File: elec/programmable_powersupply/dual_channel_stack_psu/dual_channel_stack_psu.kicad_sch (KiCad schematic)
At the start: 40 parts, among them J1 Conn_01x03_Pin, J2 Conn_01x05, Q1 Q_NMOS_GDS, Q2 Q_NMOS_GDS

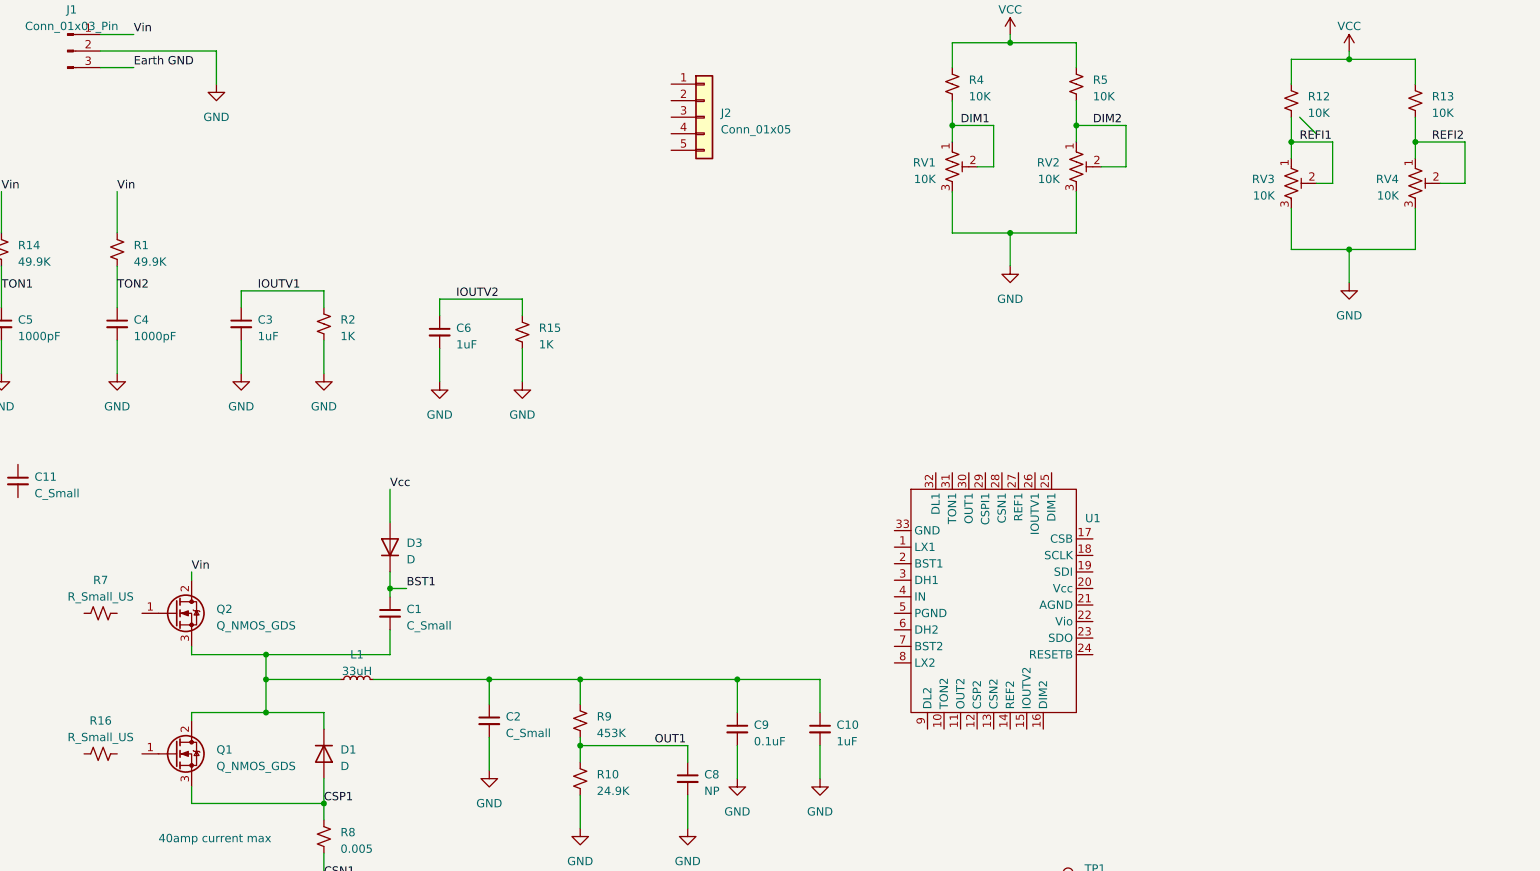
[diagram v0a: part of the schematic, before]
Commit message: added P&ID control diagram and updated dual channel stack psu
Signed-off-by: lokimetasmith <lokimail@gmail.com>
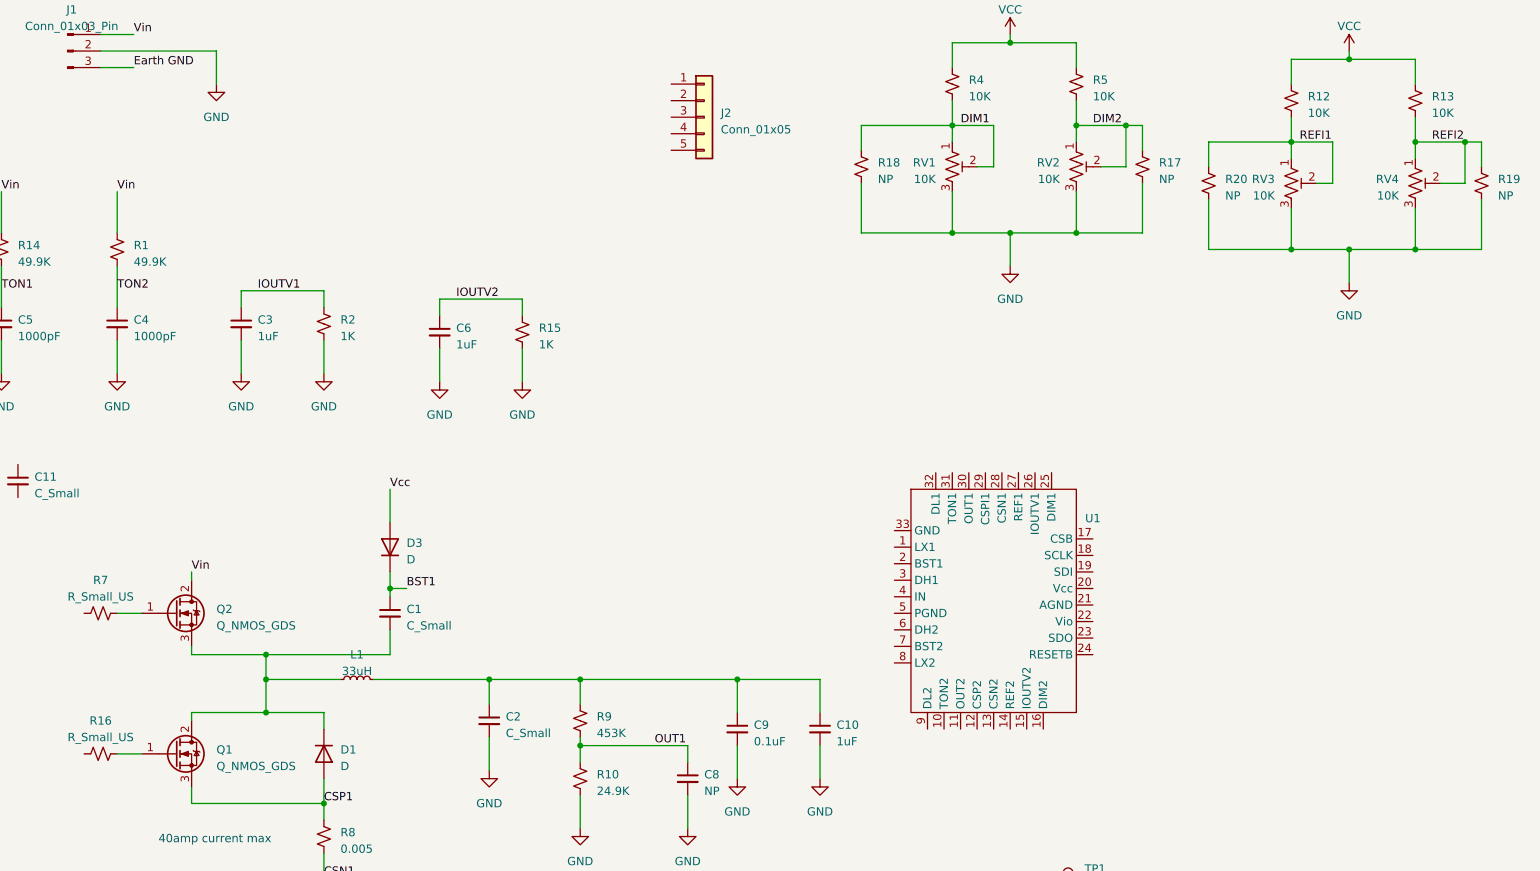
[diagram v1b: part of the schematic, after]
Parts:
- added R17, R18, R19, R20: NP, symbol Device:R_Small_US
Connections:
- net DIM1: now also R18.1
- net DIM2: now also R17.1
- net GND: now also R17.2, R18.2, R19.2, R20.2
- net REFI1: now also R20.1
- net REFI2: now also R19.1
- net at Q2.1 (G): now also R7.2
- net at R16.2: now also Q1.1 (G)
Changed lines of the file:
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@@
   (junction (at 217.17 38.1) (diameter 0) (color 0 0 0 0)
   )
+  (junction (at 191.77 35.56) (diameter 0) (color 0 0 0 0)
+  )
   (junction (at 107.95 130.81) (diameter 0) (color 0 0 0 0)
   )
@@
   (junction (at 59.69 116.84) (diameter 0) (color 0 0 0 0)
   )
+  (junction (at 236.22 54.61) (diameter 0) (color 0 0 0 0)
+  )
   (junction (at 132.08 120.65) (diameter 0) (color 0 0 0 0)
   )
   (junction (at 59.69 120.65) (diameter 0) (color 0 0 0 0)
   )
+  (junction (at 184.15 52.07) (diameter 0) (color 0 0 0 0)
+  )
   (junction (at 173.99 52.07) (diameter 0) (color 0 0 0 0)
   )
+  (junction (at 243.84 38.1) (diameter 0) (color 0 0 0 0)
+  )
   (junction (at 236.22 38.1) (diameter 0) (color 0 0 0 0)
   )
+  (junction (at 217.17 54.61) (diameter 0) (color 0 0 0 0)
+  )
   (junction (at 184.15 35.56) (diameter 0) (color 0 0 0 0)
   )
   (junction (at 173.99 22.86) (diameter 0) (color 0 0 0 0)
   )
+  (junction (at 165.1 52.07) (diameter 0) (color 0 0 0 0)
+  )
   (junction (at 59.69 125.73) (diameter 0) (color 0 0 0 0)
   )
   (junction (at 165.1 35.56) (diameter 0) (color 0 0 0 0)
   )
-  (bus_entry (at 218.44 34.29) (size 2.54 2.54)
-    (stroke (width 0) (type default))
-  )
   (wire (pts (xy 191.77 41.91) (xy 187.96 41.91))
     (stroke (width 0) (type default))
   )
+  (wire (pts (xy 194.31 52.07) (xy 184.15 52.07))
+    (stroke (width 0) (type default))
+  )
   (wire (pts (xy 124.46 133.35) (xy 124.46 130.81))
     (stroke (width 0) (type default))
@@
     (stroke (width 0) (type default))
   )
+  (wire (pts (xy 151.13 44.45) (xy 151.13 52.07))
+    (stroke (width 0) (type default))
+  )
   (wire (pts (xy 107.95 130.81) (xy 107.95 133.35))
     (stroke (width 0) (type default))
@@
     (stroke (width 0) (type default))
   )
+  (wire (pts (xy 204.47 46.99) (xy 204.47 54.61))
+    (stroke (width 0) (type default))
+  )
   (wire (pts (xy 99.06 64.77) (xy 99.06 62.23))
     (stroke (width 0) (type default))
@@
     (stroke (width 0) (type default))
   )
+  (wire (pts (xy 151.13 35.56) (xy 151.13 39.37))
+    (stroke (width 0) (type default))
+  )
   (wire (pts (xy 68.58 147.32) (xy 68.58 152.4))
     (stroke (width 0) (type default))
@@
     (stroke (width 0) (type default))
   )
+  (wire (pts (xy 246.38 38.1) (xy 246.38 41.91))
+    (stroke (width 0) (type default))
+  )
   (wire (pts (xy 226.06 54.61) (xy 226.06 59.69))
     (stroke (width 0) (type default))
@@
     (stroke (width 0) (type default))
   )
+  (wire (pts (xy 194.31 44.45) (xy 194.31 52.07))
+    (stroke (width 0) (type default))
+  )
   (wire (pts (xy 223.52 44.45) (xy 223.52 38.1))
     (stroke (width 0) (type default))
@@
     (stroke (width 0) (type default))
   )
+  (wire (pts (xy 236.22 54.61) (xy 246.38 54.61))
+    (stroke (width 0) (type default))
+  )
+  (wire (pts (xy 204.47 38.1) (xy 204.47 41.91))
+    (stroke (width 0) (type default))
+  )
   (wire (pts (xy 48.26 125.73) (xy 59.69 125.73))
     (stroke (width 0) (type default))
@@
     (stroke (width 0) (type default))
   )
+  (wire (pts (xy 204.47 38.1) (xy 217.17 38.1))
+    (stroke (width 0) (type default))
+  )
   (wire (pts (xy 184.15 52.07) (xy 173.99 52.07))
     (stroke (width 0) (type default))
@@
     (stroke (width 0) (type default))
   )
+  (wire (pts (xy 36.83 110.49) (xy 40.64 110.49))
+    (stroke (width 0) (type default))
+  )
   (wire (pts (xy 78.74 116.84) (xy 78.74 113.03))
     (stroke (width 0) (type default))
@@
     (stroke (width 0) (type default))
   )
+  (wire (pts (xy 243.84 38.1) (xy 246.38 38.1))
+    (stroke (width 0) (type default))
+  )
   (wire (pts (xy 59.69 116.84) (xy 48.26 116.84))
     (stroke (width 0) (type default))
@@
     (stroke (width 0) (type default))
   )
+  (wire (pts (xy 191.77 35.56) (xy 194.31 35.56))
+    (stroke (width 0) (type default))
+  )
+  (wire (pts (xy 246.38 46.99) (xy 246.38 54.61))
+    (stroke (width 0) (type default))
+  )
   (wire (pts (xy 165.1 26.67) (xy 165.1 22.86))
     (stroke (width 0) (type default))
@@
     (stroke (width 0) (type default))
   )
+  (wire (pts (xy 194.31 35.56) (xy 194.31 39.37))
+    (stroke (width 0) (type default))
+  )
   (wire (pts (xy 132.08 130.81) (xy 132.08 135.89))
     (stroke (width 0) (type default))
   )
+  (wire (pts (xy 151.13 52.07) (xy 165.1 52.07))
+    (stroke (width 0) (type default))
+  )
   (wire (pts (xy 184.15 45.72) (xy 184.15 52.07))
     (stroke (width 0) (type default))
@@
     (stroke (width 0) (type default))
   )
+  (wire (pts (xy 151.13 35.56) (xy 165.1 35.56))
+    (stroke (width 0) (type default))
+  )
   (wire (pts (xy 226.06 24.13) (xy 226.06 25.4))
     (stroke (width 0) (type default))
@@
     (stroke (width 0) (type default))
   )
+  (wire (pts (xy 204.47 54.61) (xy 217.17 54.61))
+    (stroke (width 0) (type default))
+  )
   (wire (pts (xy 93.98 129.54) (xy 93.98 134.62))
     (stroke (width 0) (type default))
@@
   )
   (wire (pts (xy 86.36 69.85) (xy 86.36 74.93))
+    (stroke (width 0) (type default))
+  )
+  (wire (pts (xy 36.83 132.08) (xy 40.64 132.08))
     (stroke (width 0) (type default))
   )
@@
     )
   )
+  (symbol (lib_id "Device:R_Small_US") (at 194.31 41.91 0) (unit 1)
+    (in_bom yes) (on_board yes) (dnp no) (fields_autoplaced)
+    (property "Reference" "R17" (at 196.85 41.275 0)
+      (effects (font (size 1.27 1.27)) (justify left))
+    )
+    (property "Value" "NP" (at 196.85 43.815 0)
+      (effects (font (size 1.27 1.27)) (justify left))
+    )
+    (property "Footprint" "" (at 194.31 41.91 0)
+      (effects (font (size 1.27 1.27)) hide)
+    )
+    (property "Datasheet" "~" (at 194.31 41.91 0)
+      (effects (font (size 1.27 1.27)) hide)
+    )
+    (pin "1")
+    (pin "2")
+    (instances
+      (project "dual_channel_stack_psu"
+        (path "/8f6d02f7-7b5e-4155-bbdb-2d46789ca027"
+          (reference "R17") (unit 1)
+        )
+      )
+    )
+  )
   (symbol (lib_id "Device:R_Small_US") (at 36.83 54.61 0) (unit 1)
     (in_bom yes) (on_board yes) (dnp no) (fields_autoplaced)
@@
     )
   )
+  (symbol (lib_id "Device:R_Small_US") (at 151.13 41.91 0) (unit 1)
+    (in_bom yes) (on_board yes) (dnp no) (fields_autoplaced)
+    (property "Reference" "R18" (at 153.67 41.275 0)
+      (effects (font (size 1.27 1.27)) (justify left))
+    )
+    (property "Value" "NP" (at 153.67 43.815 0)
+      (effects (font (size 1.27 1.27)) (justify left))
+    )
+    (property "Footprint" "" (at 151.13 41.91 0)
+      (effects (font (size 1.27 1.27)) hide)
+    )
+    (property "Datasheet" "~" (at 151.13 41.91 0)
+      (effects (font (size 1.27 1.27)) hide)
+    )
+    (pin "1")
+    (pin "2")
+    (instances
+      (project "dual_channel_stack_psu"
+        (path "/8f6d02f7-7b5e-4155-bbdb-2d46789ca027"
+          (reference "R18") (unit 1)
+        )
+      )
+    )
+  )
   (symbol (lib_id "Device:C_Small") (at 55.88 66.04 0) (unit 1)
     (in_bom yes) (on_board yes) (dnp no) (fields_autoplaced)
@@
         (path "/8f6d02f7-7b5e-4155-bbdb-2d46789ca027"
           (reference "#PWR015") (unit 1)
+        )
+      )
+    )
+  )
+  (symbol (lib_id "Device:R_Small_US") (at 246.38 44.45 0) (unit 1)
+    (in_bom yes) (on_board yes) (dnp no) (fields_autoplaced)
+    (property "Reference" "R19" (at 248.92 43.815 0)
+      (effects (font (size 1.27 1.27)) (justify left))
+    )
+    (property "Value" "NP" (at 248.92 46.355 0)
+      (effects (font (size 1.27 1.27)) (justify left))
+    )
+    (property "Footprint" "" (at 246.38 44.45 0)
+      (effects (font (size 1.27 1.27)) hide)
+    )
+    (property "Datasheet" "~" (at 246.38 44.45 0)
+      (effects (font (size 1.27 1.27)) hide)
+    )
+    (pin "1")
+    (pin "2")
+    (instances
+      (project "dual_channel_stack_psu"
+        (path "/8f6d02f7-7b5e-4155-bbdb-2d46789ca027"
+          (reference "R19") (unit 1)
         )
       )
@@
         )
       )
+    )
+  )
+  (symbol (lib_id "Device:R_Small_US") (at 204.47 44.45 0) (unit 1)
+    (in_bom yes) (on_board yes) (dnp no) (fields_autoplaced)
+    (property "Reference" "R20" (at 207.01 43.815 0)
+      (effects (font (size 1.27 1.27)) (justify left))
+    )
+    (property "Value" "NP" (at 207.01 46.355 0)
+      (effects (font (size 1.27 1.27)) (justify left))
+    )
+    (property "Footprint" "" (at 204.47 44.45 0)
+      (effects (font (size 1.27 1.27)) hide)
+    )
+    (property "Datasheet" "~" (at 204.47 44.45 0)
+      (effects (font (size 1.27 1.27)) hide)
+    )
+    (pin "1")
+    (pin "2")
+    (instances
+      (project "dual_channel_stack_psu"
+        (path "/8f6d02f7-7b5e-4155-bbdb-2d46789ca027"
+          (reference "R20") (unit 1)
+        )
+      )

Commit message: updated SBC setup instructions
Signed-off-by: lokimetasmith <lokimail@gmail.com>
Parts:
- added J10, J3, J6, J7: Conn_01x10, Connector_PinSocket_2.54mm:PinSocket_1x10_P2.54mm_Vertical, symbol Connector_Generic:Conn_01x10
- added J4, J8: Conn_02x12_Odd_Even, PubInv_KiCad_PCB.pretty:PinHeader_2x12_P2.00mm_Vertical_JST, symbol Connector_Generic:Conn_02x12_Odd_Even
- added J5, J9: Screw_Terminal_01x02, TerminalBlock_TE-Connectivity:TerminalBlock_TE_282834-2_1x02_P2.54mm_Horizontal, symbol Connector:Screw_Terminal_01x02
- added JP1, JP2: SolderJumper_2_Open, symbol Jumper:SolderJumper_2_Open
- added Q601 (x2): BSS138, Package_TO_SOT_SMD:SOT-23, symbol Transistor_FET:BSS138
- added R101 (x12): 1R0, Resistor_SMD:R_0603_1608Metric_Pad0.98x0.95mm_HandSolder, symbol Device:R
- added R102 (x2): 10K, Resistor_SMD:R_0603_1608Metric_Pad0.98x0.95mm_HandSolder, symbol Device:R
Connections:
- net GND: now also J3.2 (Pin_2), J3.3 (Pin_3), J3.5 (Pin_5), J3.7 (Pin_7), J3.8 (Pin_8), J3.9 (Pin_9), J4.10 (Pin_10), J4.14 (Pin_14), J4.16 (Pin_16), J4.18 (Pin_18), J4.22 (Pin_22), J4.4 (Pin_4), J4.6 (Pin_6), J7.3 (Pin_3), J7.5 (Pin_5), J7.7 (Pin_7), J7.8 (Pin_8), J7.9 (Pin_9), J8.10 (Pin_10), J8.14 (Pin_14), J8.16 (Pin_16), J8.18 (Pin_18), J8.22 (Pin_22), J8.6 (Pin_6), Q601.2 (S), Q601.2 (S), R102.2, R102.2
- net VO+: now reaches C10.1, C2.1, C9.1, L1.2
- net VO+: now also J3.1 (Pin_1), J4.2 (Pin_2), JP1.2 (B); no longer R9.1
- new net: Q601.1 (G), R102.1
- new net ACI: J4.13 (Pin_13), J6.7 (Pin_7)
- new net ACI2: J10.7 (Pin_7), J8.13 (Pin_13)
- new net AUX: J3.6 (Pin_6), J4.12 (Pin_12), J4.17 (Pin_17), J4.21 (Pin_21), J6.10 (Pin_10), J6.9 (Pin_9), R101.1
- new net AUX2: J10.10 (Pin_10), J10.9 (Pin_9), J7.6 (Pin_6), J8.12 (Pin_12), J8.17 (Pin_17), J8.21 (Pin_21), R101.1
- new net D_PSU_RX: R101.2
- new net D_PSU_RX2: R101.2
- new net D_PSU_TX: R101.1
- new net D_PSU_TX2: R101.1
- new net EN+: J4.11 (Pin_11), J6.6 (Pin_6), R101.2
- new net EN-: J4.9 (Pin_9), J6.5 (Pin_5), Q601.3 (D)
- new net EN2+: J10.6 (Pin_6), J8.11 (Pin_11), R101.2
- new net EN2-: J10.5 (Pin_5), J8.9 (Pin_9), Q601.3 (D)
- new net PAR: J4.7 (Pin_7), J6.4 (Pin_4)
- new net PAR2: J10.4 (Pin_4), J8.7 (Pin_7)
- new net POK: J4.5 (Pin_5), J6.3 (Pin_3)
- new net POK2: J10.3 (Pin_3), J8.5 (Pin_5)
- new net PS1_EN: Q601.1 (G), R102.1
- new net PS2_SCL: J8.19 (Pin_19), R101.2
- new net PS2_SDA: J7.10 (Pin_10), J8.20 (Pin_20), R101.1
- new net PS_SCL: J4.19 (Pin_19), R101.2
- new net PS_SDA: J3.10 (Pin_10), J4.20 (Pin_20), R101.1
- new net RX: J4.23 (Pin_23), R101.2
- new net RX2: J8.23 (Pin_23), R101.2
- new net SCL: R101.1, R101.1
- new net SDA: R101.2, R101.2
- new net TX: J4.24 (Pin_24), R101.1
- new net TX2: J8.24 (Pin_24), R101.1
- new net VCI: J4.15 (Pin_15), J6.8 (Pin_8)
- new net VCI2: J10.8 (Pin_8), J8.15 (Pin_15)
- new net VO2+: J7.1 (Pin_1), J8.2 (Pin_2)
- new net VO2-: J7.2 (Pin_2), J8.4 (Pin_4)
- new net VS+: J4.1 (Pin_1), J5.1 (Pin_1), J6.1 (Pin_1)
- new net VS-: J4.3 (Pin_3), J5.2 (Pin_2), J6.2 (Pin_2)
- new net VS2+: J10.1 (Pin_1), J8.1 (Pin_1), J9.1 (Pin_1)
- new net VS2-: J10.2 (Pin_2), J8.3 (Pin_3), J9.2 (Pin_2)
- new net VSET: J3.4 (Pin_4), J4.8 (Pin_8)
- new net VSET2: J7.4 (Pin_4), J8.8 (Pin_8)
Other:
- note added: "NULL MODEM here."
- note added: "Power supply control 1"
- note added: "Power supply control 2"
- note added: "Remote Sense 1"
- note added: "Remote Sense 2"
- moved on the sheet: C8, R10, R11, R3, R9
